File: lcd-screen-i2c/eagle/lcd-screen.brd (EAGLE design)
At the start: 99.1 x 73.7 mm, 29 parts, among them CON1 SPI, IC1 MCP1703CB, J1 RJ12RIGHTANGLE-I2C, J2 RJ12RIGHTANGLE-I2C, J3 RJ12RIGHTANGLE-I2C, U1 ATMEGA328P_TQFP, X1 8MHz

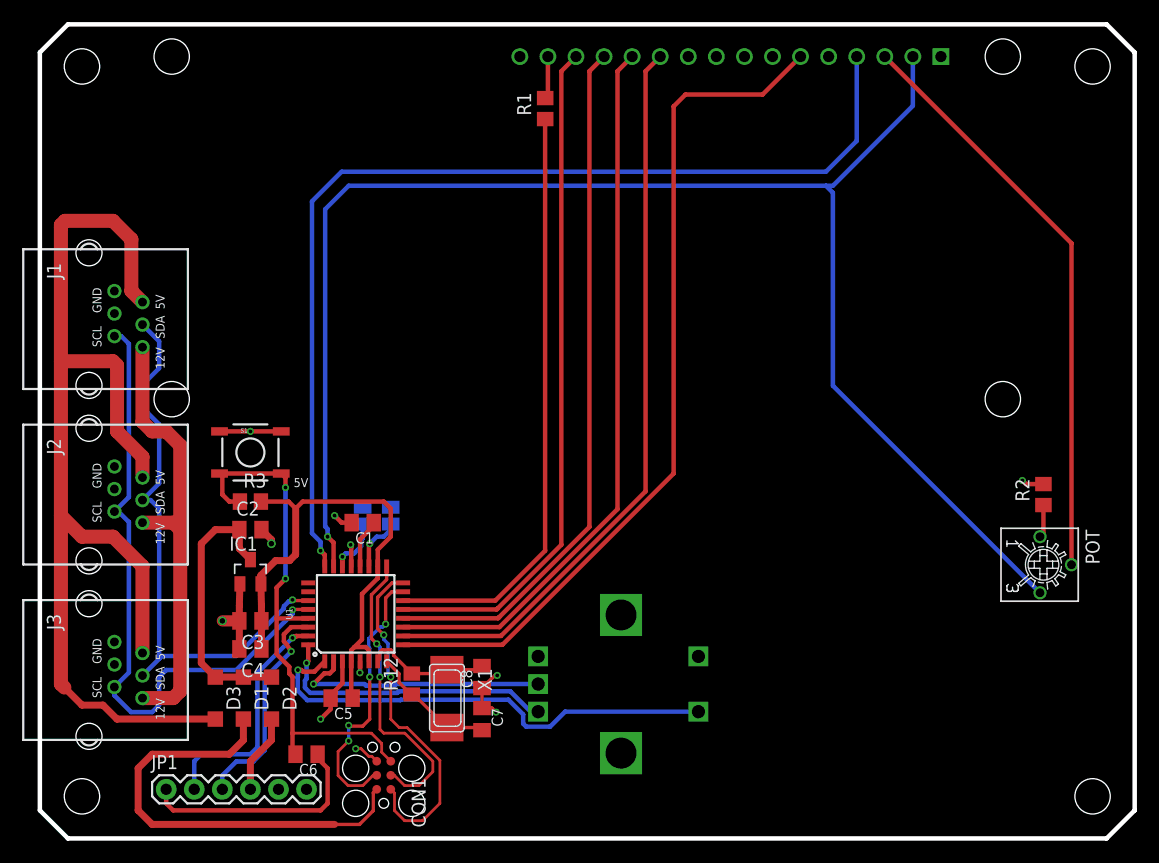
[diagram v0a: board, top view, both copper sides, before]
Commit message: Change rotary encoder pinout to use interruptible pins on Atmega328p
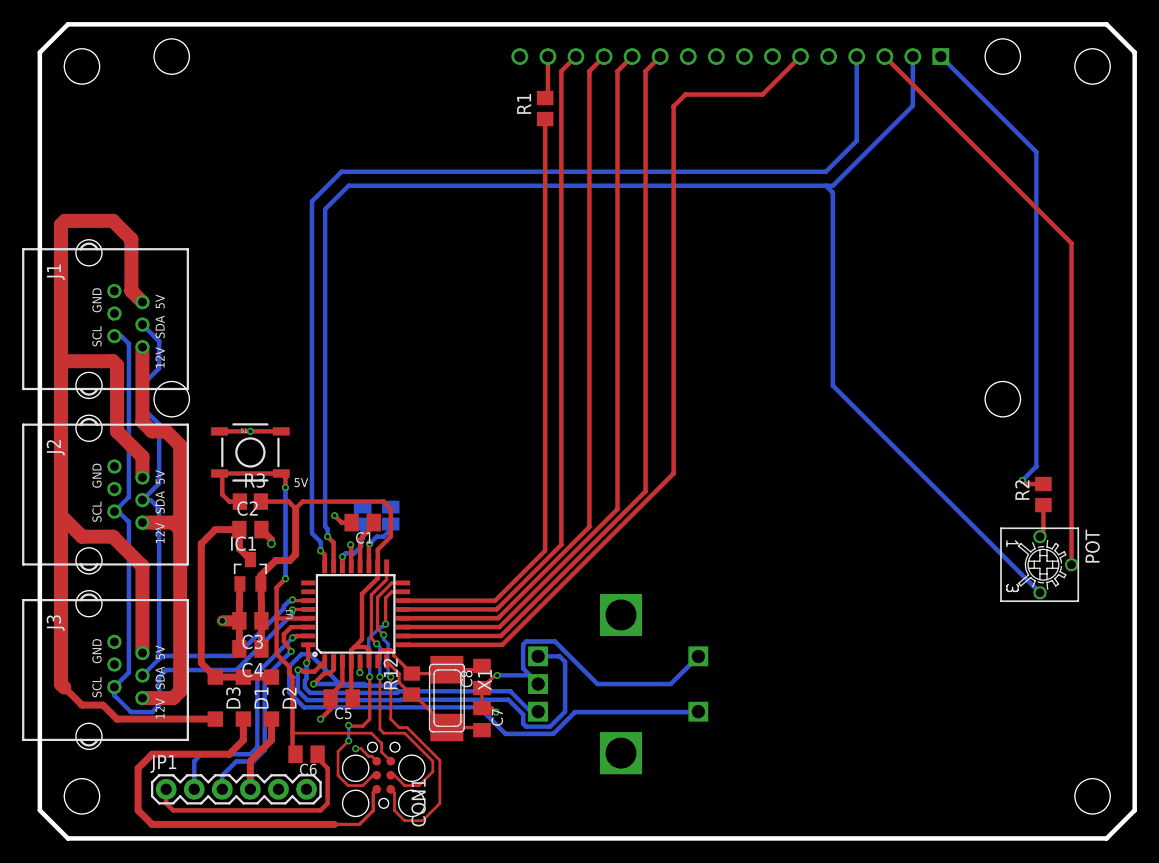
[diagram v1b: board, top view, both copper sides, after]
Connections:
- net D3: now also U$1.C; no longer U$1.D
- net D4: now also U$1.D; no longer U$1.B
- net GND: now also U$1.B; no longer U$1.C
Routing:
- net GND: track 35.0 -> 104.3 mm
- net D4: track 23.5 -> 61.0 mm
- net D3: track 43.4 -> 38.6 mm
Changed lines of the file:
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@@
 <contactref element="LCD" pad="16"/>
 <contactref element="R2" pad="2"/>
-<contactref element="U$1" pad="C"/>
 <contactref element="U$1" pad="E"/>
 <contactref element="C5" pad="2"/>
@@
 <wire x1="27.305" y1="28.575" x2="26.67" y2="29.21" width="0.4064" layer="1"/>
 <via x="26.67" y="29.21" extent="1-16" drill="0.35"/>
+<contactref element="U$1" pad="B"/>
+<wire x1="41.3824" y1="14.7506" x2="44.3044" y2="14.7506" width="0.4064" layer="16"/>
+<wire x1="44.3044" y1="14.7506" x2="45.085" y2="13.97" width="0.4064" layer="16"/>
+<wire x1="57.085" y1="13.97" x2="59.585" y2="16.47" width="0.4064" layer="16"/>
+<wire x1="43.7318" y1="15.38228125" x2="43.7318" y2="17.55771875" width="0.4064" layer="16"/>
+<wire x1="43.7318" y1="17.55771875" x2="43.99728125" y2="17.8232" width="0.4064" layer="16"/>
+<wire x1="50.45829375" y1="13.97" x2="57.085" y2="13.97" width="0.4064" layer="16"/>
+<wire x1="43.99728125" y1="17.8232" x2="46.60509375" y2="17.8232" width="0.4064" layer="16"/>
+<wire x1="46.60509375" y1="17.8232" x2="50.45829375" y2="13.97" width="0.4064" layer="16"/>
+<wire x1="45.085" y1="13.97" x2="45.085" y2="14.02908125" width="0.4064" layer="16"/>
+<wire x1="45.085" y1="14.02908125" x2="43.7318" y2="15.38228125" width="0.4064" layer="16"/>
+<wire x1="81.53" y1="70.745" x2="90.17" y2="62.105" width="0.4064" layer="16"/>
+<wire x1="90.17" y1="33.655" x2="88.9" y2="32.385" width="0.4064" layer="16"/>
+<wire x1="90.17" y1="62.105" x2="90.17" y2="33.655" width="0.4064" layer="16"/>
 </signal>
 <signal name="SCK">
@@
 </signal>
 <signal name="D3">
-<contactref element="U$1" pad="D"/>
 <wire x1="46.17271875" y1="10.1168" x2="43.99728125" y2="10.1168" width="0.4064" layer="16"/>
 <wire x1="43.99728125" y1="10.1168" x2="43.7318" y2="10.38228125" width="0.4064" layer="16"/>
 <wire x1="43.7318" y1="10.38228125" x2="43.7318" y2="11.21990625" width="0.4064" layer="16"/>
 <wire x1="43.7318" y1="11.21990625" x2="42.398353125" y2="12.553353125" width="0.4064" layer="16"/>
-<wire x1="59.585" y1="11.47" x2="47.52591875" y2="11.47" width="0.4064" layer="16"/>
-<wire x1="47.52591875" y1="11.47" x2="46.17271875" y2="10.1168" width="0.4064" layer="16"/>
+<wire x1="46.17271875" y1="10.1168" x2="47.52591875" y2="11.47" width="0.4064" layer="16"/>
 <wire x1="42.398353125" y1="12.553353125" x2="32.658878125" y2="12.553353125" width="0.4064" layer="16"/>
 <wire x1="32.658878125" y1="12.553353125" x2="32.617125" y2="12.5116" width="0.4064" layer="16"/>
@@
 <contactref element="U1" pad="1"/>
 <wire x1="25.775" y1="16.0274" x2="24.842" y2="15.0944" width="0.4064" layer="1"/>
+<contactref element="U$1" pad="C"/>
+<wire x1="47.52591875" y1="11.47" x2="47.52591875" y2="15.97408125" width="0.4064" layer="16"/>
+<wire x1="47.52591875" y1="15.97408125" x2="46.99" y2="16.51" width="0.4064" layer="16"/>
+<wire x1="46.99" y1="16.51" x2="46.95" y2="16.47" width="0.4064" layer="16"/>
+<wire x1="46.95" y1="16.47" x2="45.085" y2="16.47" width="0.4064" layer="16"/>
 </signal>
 <signal name="D4">
-<contactref element="U$1" pad="B"/>
-<wire x1="45.085" y1="13.97" x2="32.2189375" y2="13.97" width="0.4064" layer="16"/>
 <wire x1="32.2189375" y1="13.97" x2="32.0733375" y2="13.8244" width="0.4064" layer="16"/>
 <wire x1="29.5216625" y1="13.8244" x2="29.3760625" y2="13.97" width="0.4064" layer="16"/>
@@
 <wire x1="26.575" y1="16.0274" x2="26.575" y2="15.27208125" width="0.4064" layer="1"/>
 <wire x1="26.575" y1="15.27208125" x2="26.24211875" y2="14.9392" width="0.4064" layer="1"/>
+<contactref element="U$1" pad="D"/>
+<wire x1="46.4446125" y1="9.4604" x2="48.4142125" y2="11.43" width="0.4064" layer="16"/>
+<wire x1="29.5216625" y1="13.8244" x2="27.2845375" y2="13.8244" width="0.4064" layer="16"/>
+<wire x1="27.2845375" y1="13.8244" x2="24.4533375" y2="16.6556" width="0.4064" layer="16"/>
+<wire x1="23.919275" y1="11.8552" x2="39.7458625" y2="11.8552" width="0.4064" layer="16"/>
+<wire x1="24.4533375" y1="16.6556" x2="23.6610625" y2="16.6556" width="0.4064" layer="16"/>
+<wire x1="23.6610625" y1="16.6556" x2="22.5688" y2="15.5633375" width="0.4064" layer="16"/>
+<wire x1="22.5688" y1="15.5633375" x2="22.5688" y2="13.205675" width="0.4064" layer="16"/>
+<wire x1="22.5688" y1="13.205675" x2="23.919275" y2="11.8552" width="0.4064" layer="16"/>
+<wire x1="39.7458625" y1="11.8552" x2="42.1406625" y2="9.4604" width="0.4064" layer="16"/>
+<wire x1="42.1406625" y1="9.4604" x2="46.4446125" y2="9.4604" width="0.4064" layer="16"/>
+<wire x1="59.545" y1="11.43" x2="59.585" y2="11.47" width="0.4064" layer="16"/>
+<wire x1="48.4142125" y1="11.43" x2="59.545" y2="11.43" width="0.4064" layer="16"/>
 </signal>
 <signal name="D5">
